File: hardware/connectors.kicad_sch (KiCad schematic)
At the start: 12 parts, among them J3 54601-906WPLF, J4 54-00174 / FC68125, J5 54-00174 / FC68125, J6 54-00174 / FC68125, J8 54-00174 / FC68125, J9 54-00174 / FC68125, U4 D1213A-04SO-7, U6 D1213A-04SO-7, U7 D1213A-04SO-7

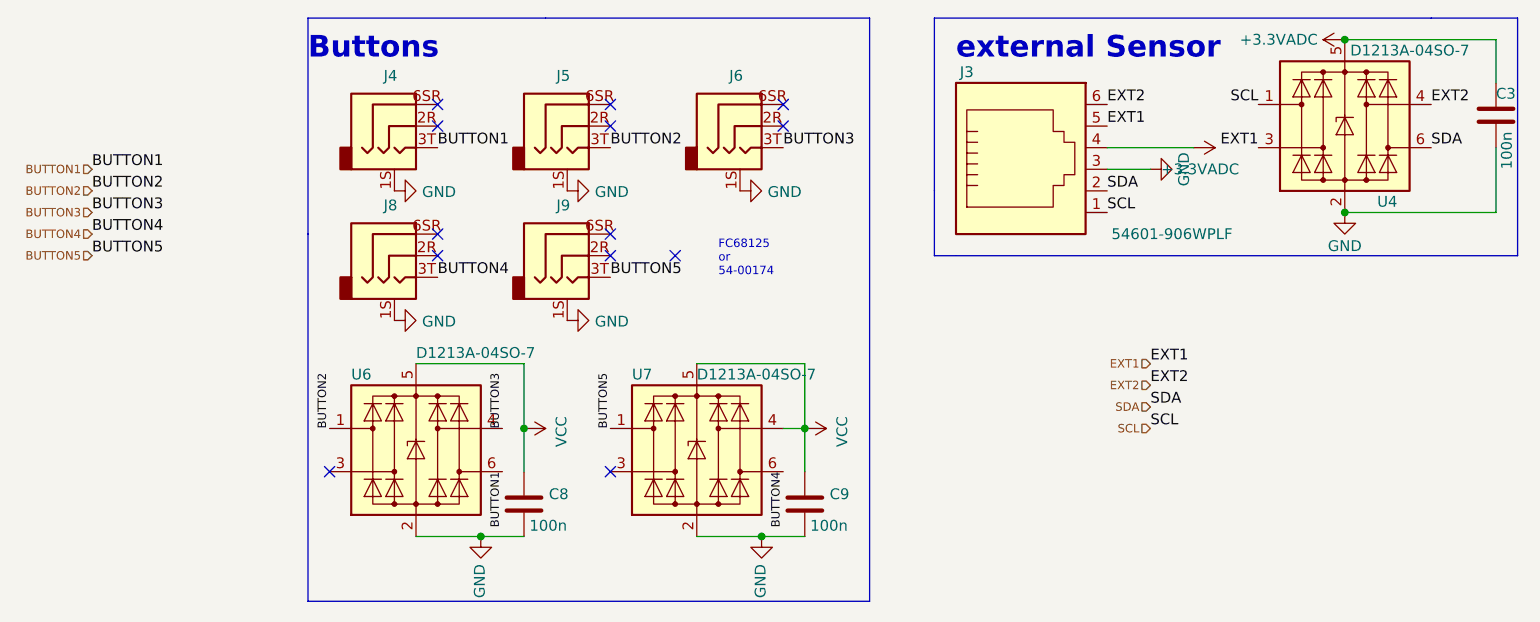
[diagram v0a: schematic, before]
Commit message: Fixed some messed up labels (imports from EAGLE); cleaned up unused libs
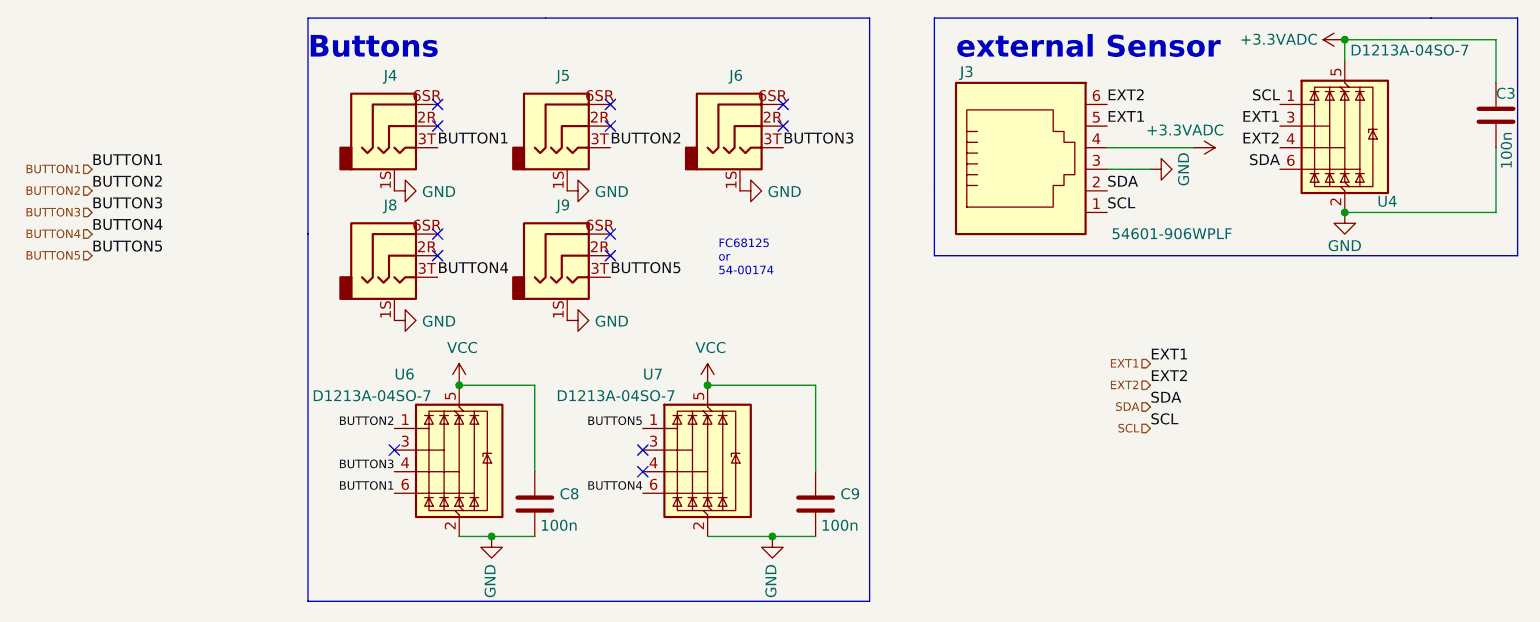
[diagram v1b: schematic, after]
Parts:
- U4, U6, U7: footprint Package_TO_SOT_SMD:SC-74-6_1.55x2.9mm_P0.95mm -> Package_TO_SOT_SMD:SOT-23-6
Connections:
- net VCC: no longer U7.4 (I/O3)
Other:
- moved on the sheet: C8, C9

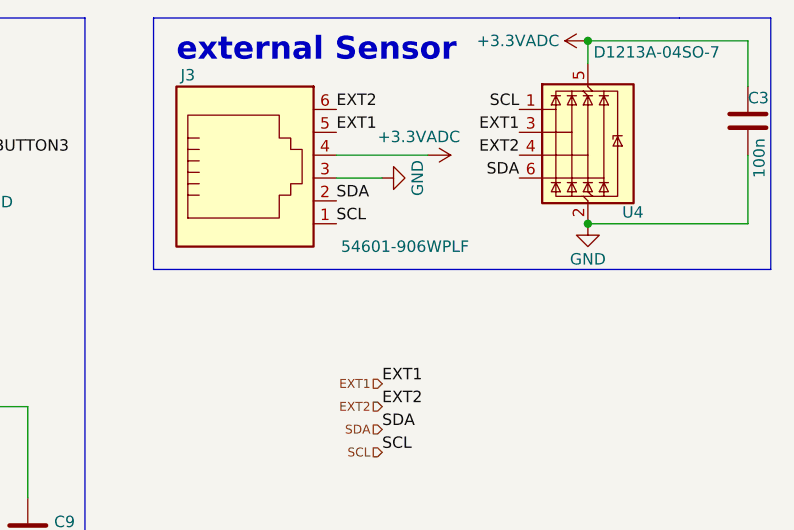
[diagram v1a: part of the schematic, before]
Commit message: Replaced RJ12 connector value (not available anymore); cleanup of iBOM, removed unused old csv/ods BOM
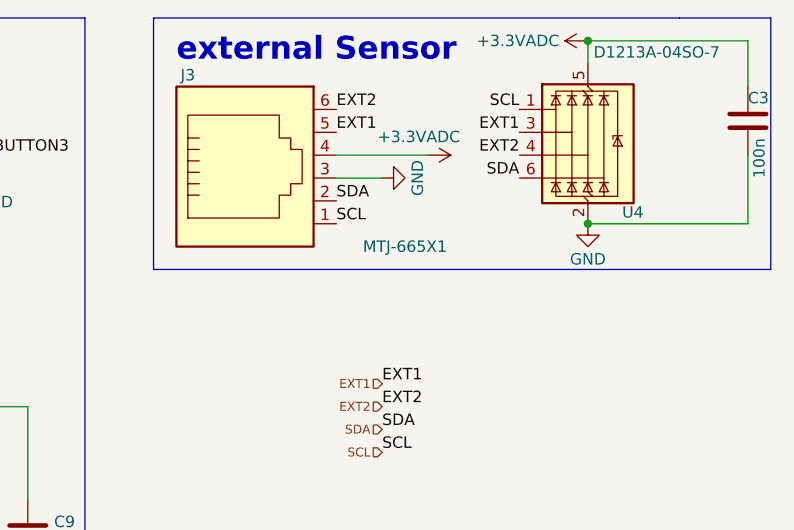
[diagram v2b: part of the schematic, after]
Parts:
- J3: value 54601-906WPLF -> MTJ-665X1; Digikey 609-4729-ND -> 2057-MTJ-665X1-ND; Farnell 2135977 -> (none); Mouser 649-54601-906WPLF -> 737-MTJ-665X1
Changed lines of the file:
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@@
 			)
 		)
-		(property "Value" "54601-906WPLF"
+		(property "Value" "MTJ-665X1"
 			(at 190.5 50.8 0)
 			(effects
@@
 			)
 		)
-		(property "Digikey" "609-4729-ND"
+		(property "Digikey" "2057-MTJ-665X1-ND"
 			(at 172.72 43.18 0)
 			(effects
@@
 			)
 		)
-		(property "Farnell" "2135977"
+		(property "Farnell" ""
 			(at 172.72 43.18 0)
 			(effects
@@
 			)
 		)
-		(property "Mouser" " 649-54601-906WPLF"
+		(property "Mouser" "737-MTJ-665X1"
 			(at 172.72 43.18 0)
 			(effects

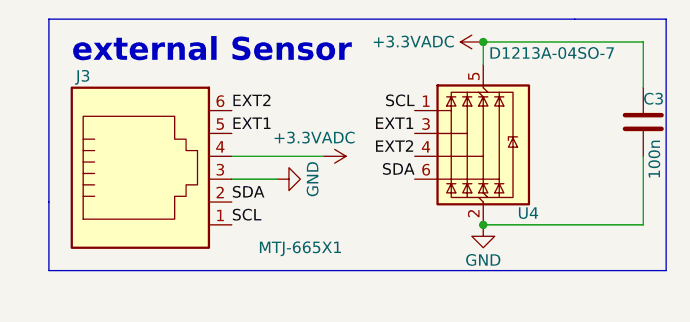
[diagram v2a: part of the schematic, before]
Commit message: Changed VCC of TVS array from LDO 3V3ADC to VCC (always on), prevents leackage current when LDO is switched off and pullups are on any EXT GPIO pin
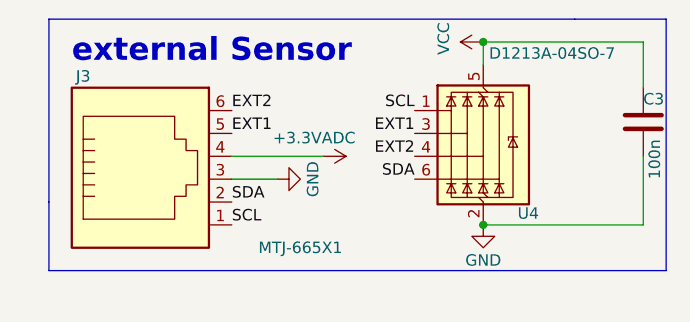
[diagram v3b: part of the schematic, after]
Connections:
- net +3.3VADC: no longer C3.1, U4.5 (VBUS)
- net VCC: now also C3.1, U4.5 (VBUS)
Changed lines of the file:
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@@
+	)
+	(junction
+		(at 210.82 27.94)
+		(diameter 0)
+		(color 0 0 0 0)
 	)
 	(junction
@@
 	(junction
 		(at 135.89 68.58)
-		(diameter 0)
-		(color 0 0 0 0)
-	)
-	(junction
-		(at 210.82 27.94)
 		(diameter 0)
 		(color 0 0 0 0)
@@
 	)
 	(symbol
-		(lib_id "power:+3.3VADC")
-		(at 210.82 27.94 90)
-		(unit 1)
-		(exclude_from_sim no)
-		(in_bom yes)
-		(on_board yes)
-		(dnp no)
-		(property "Reference" "#PWR0104"
-			(at 212.09 24.13 0)
-			(effects
-				(font
-					(size 1.27 1.27)
-				)
-				(hide yes)
-			)
-		)
-		(property "Value" "+3.3VADC"
-			(at 207.645 27.94 90)
-			(effects
-				(font
-					(size 1.27 1.27)
-				)
-				(justify left)
-			)
-		)
-		(property "Footprint" ""
-			(at 210.82 27.94 0)
-			(effects
-				(font
-					(size 1.27 1.27)
-				)
-				(hide yes)
-			)
-		)
-		(property "Datasheet" ""
-			(at 210.82 27.94 0)
-			(effects
-				(font
-					(size 1.27 1.27)
-				)
-				(hide yes)
-			)
-		)
-		(property "Description" "Power symbol creates a global label with name \"+3.3VADC\""
-			(at 210.82 27.94 0)
-			(effects
-				(font
-					(size 1.27 1.27)
-				)
-				(hide yes)
-			)
-		)
-		(pin "1"
-		)
-		(instances
-			(project "FABI_schematic"
-				(path "/8404dabe-a0ce-44ce-a3c9-f9e9e54d2b02/301e6e18-5436-47c5-b1ce-681b8073d9ea"
-					(reference "#PWR0104")
-					(unit 1)
-				)
-			)
-		)
-	)
-	(symbol
 		(lib_id "power:GND")
 		(at 99.06 60.96 90)
@@
 					(unit 1)
 				)
+			)
+		)
+	)
+	(symbol
+		(lib_id "power:VCC")
+		(at 210.82 27.94 90)
+		(unit 1)
+		(exclude_from_sim no)
+		(in_bom yes)
+		(on_board yes)
+		(dnp no)
+		(property "Reference" "#PWR055"
+			(at 214.63 27.94 0)
+			(effects
+				(font
+					(size 1.27 1.27)
+				)
+				(hide yes)
+			)
+		)
+		(property "Value" "VCC"
+			(at 206.4258 27.559 0)
+			(effects
+				(font
+					(size 1.27 1.27)
+				)
+			)
+		)
+		(property "Footprint" ""
+			(at 210.82 27.94 0)
+			(effects
+				(font
+					(size 1.27 1.27)
+				)
+				(hide yes)
+			)
+		)
+		(property "Datasheet" ""
+			(at 210.82 27.94 0)
+			(effects
+				(font
+					(size 1.27 1.27)
+				)
+				(hide yes)
+			)
+		)
+		(property "Description" "Power symbol creates a global label with name \"VCC\""
+			(at 210.82 27.94 0)
+			(effects
+				(font
+					(size 1.27 1.27)
+				)
+				(hide yes)
+			)
+		)
+		(pin "1"
+		)
+		(instances
+			(project "FABI_schematic"
+				(path "/8404dabe-a0ce-44ce-a3c9-f9e9e54d2b02/301e6e18-5436-47c5-b1ce-681b8073d9ea"
+					(reference "#PWR055")
+					(unit 1)
+				)
